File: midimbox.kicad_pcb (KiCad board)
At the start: 2 copper layers, 11 parts, among them J3 AudioJack3, J4 Conn_01x05, U1 6N138, U2 74LS00

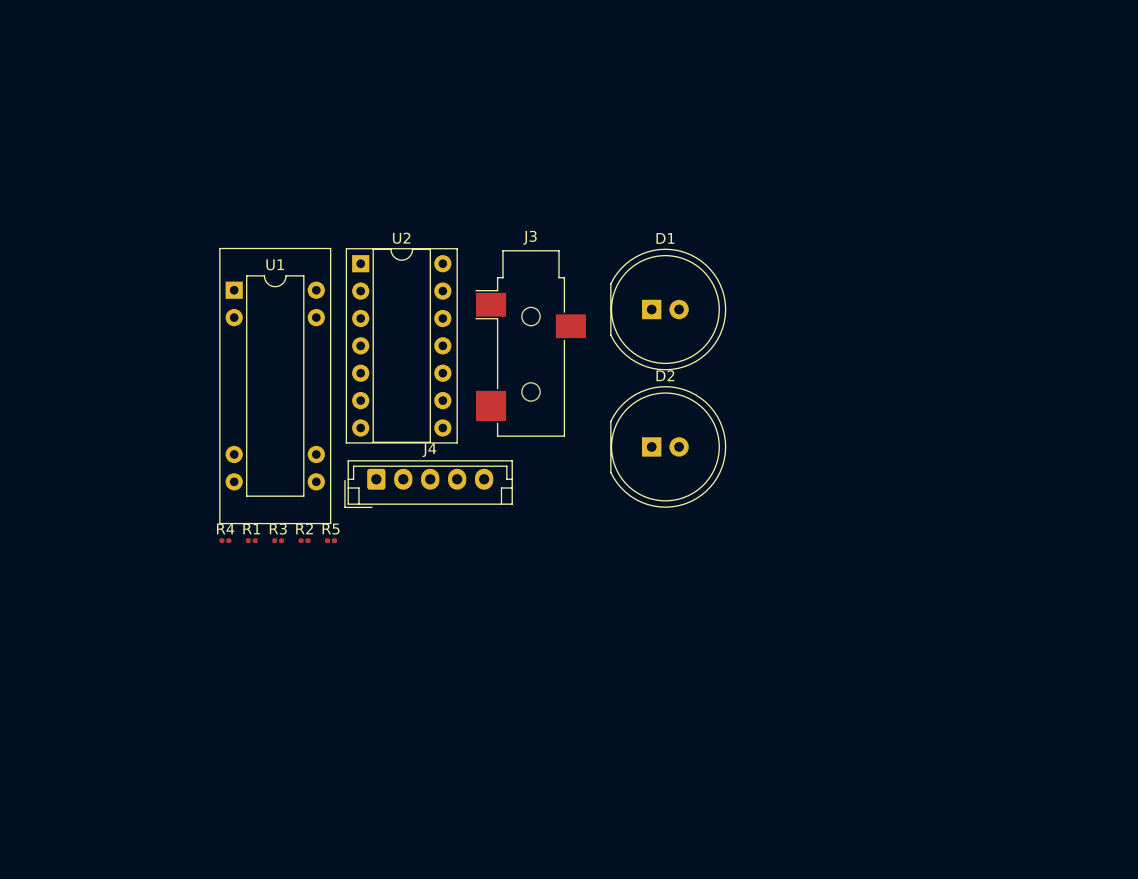
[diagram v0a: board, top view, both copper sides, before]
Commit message: Rough attempt at modelling the PCB.
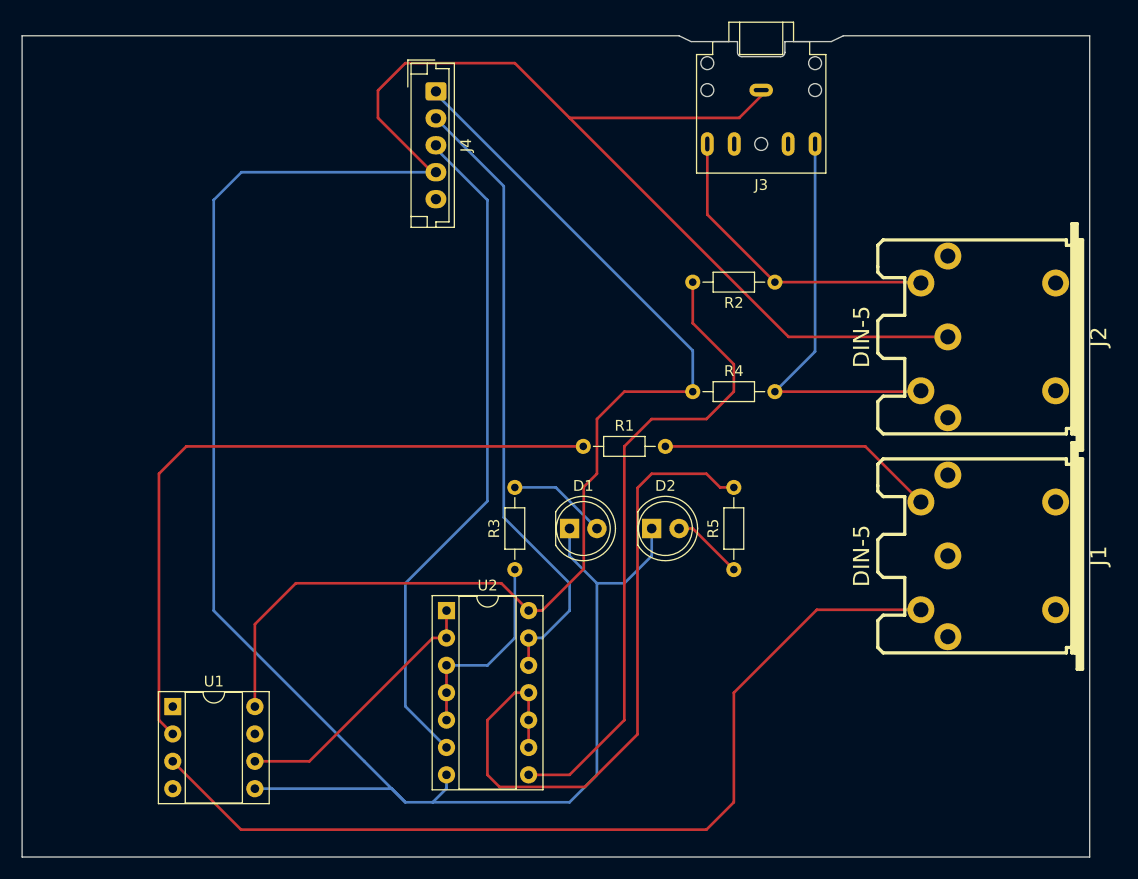
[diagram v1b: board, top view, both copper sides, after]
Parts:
- added J1: DIN-5, AVConnectors:din-5, F.Cu at (198.1, 96.5)
- added J2: DIN-5, AVConnectors:din-5, F.Cu at (198.1, 76.2)
- D1, D2: footprint LED_THT:LED_D10.0mm -> LED_THT:LED_D5.0mm
- J3: footprint Connector_Audio:Jack_3.5mm_CUI_SJ-3523-SMT_Horizontal -> Connector_Audio:Jack_3.5mm_CUI_SJ1-3525N_Horizontal
- R1, R2, R3, R4, R5: footprint Resistor_SMD:R_0201_0603Metric -> Resistor_THT:R_Axial_DIN0204_L3.6mm_D1.6mm_P7.62mm_Horizontal
- U1: footprint Package_DIP:DIP-8-16_W7.62mm_Socket -> Package_DIP:DIP-8_W7.62mm_Socket
- moved R2 49.8 mm to (179.1, 71.1), turned to 180 degrees
- moved R4 45.5 mm to (171.4, 81.3)
- moved U1 39.0 mm to (123.2, 110.5)
- moved R5 37.5 mm to (175.3, 97.8), turned to 90 degrees
- moved J4 36.4 mm to (147.6, 53.4), turned to -90 degrees
- moved U2 33.2 mm to (148.6, 101.6)
- moved R1 32.0 mm to (161.3, 86.4)
- moved J3 31.8 mm to (177.8, 53.3), turned to 180 degrees
- moved R3 22.1 mm to (154.9, 97.8), turned to 90 degrees
- moved D1 21.7 mm to (160.0, 94.0)
- moved D2 7.57 mm to (167.6, 94.0)
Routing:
- net Net-(D1-Pad1): track 0.00 -> 247.5 mm
- net Net-(J4-Pad1): track 0.00 -> 104.3 mm
- net Net-(J1-Pad5): track 0.00 -> 86.4 mm
- net Net-(R1-Pad1): track 0.00 -> 65.1 mm
- net Net-(R5-Pad2): track 0.00 -> 64.3 mm
- net Net-(J4-Pad3): track 0.00 -> 62.6 mm
- net Net-(R2-Pad2): track 0.00 -> 60.4 mm
- net Net-(J4-Pad2): track 0.00 -> 58.2 mm
- net Net-(J2-Pad5): track 0.00 -> 38.1 mm
- net Net-(J2-Pad4): track 0.00 -> 29.0 mm
- net Net-(J1-Pad4): track 0.00 -> 25.8 mm
- net Net-(U1-Pad6): track 0.00 -> 25.1 mm
- net Net-(R3-Pad1): track 0.00 -> 18.8 mm
- net Net-(D1-Pad2): track 0.00 -> 9.20 mm
- net Net-(D2-Pad2): track 0.00 -> 6.66 mm
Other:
- board outline added: 99.1 x 76.2 mm
